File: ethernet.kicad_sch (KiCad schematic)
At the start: 37 parts, among them J801 SI-60062-F, U801 USBLC6-4SC6, U802 LAN8742A-CZ-TR, Y801 Crystal_GND24

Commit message: minor formatting updates
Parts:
- renumbered C811 to C801, C812 to C802, C801 to C803, C802 to C804, C803 to C805, C808 to C806, C809 to C807, C810 to C808, C806 to C809, C807 to C810, C804 to C811, C805 to C812, R810 to R801, R815 to R802, R816 to R803, R818 to R804, R819 to R805, R805 to R806, R806 to R807, R807 to R808, R820 to R809, R808 to R810, R809 to R811, R801 to R812, R802 to R813, R803 to R814, R817 to R815, R804 to R816, R811 to R817, R812 to R818, R813 to R819, R814 to R820, U802 to U801, U801 to U802

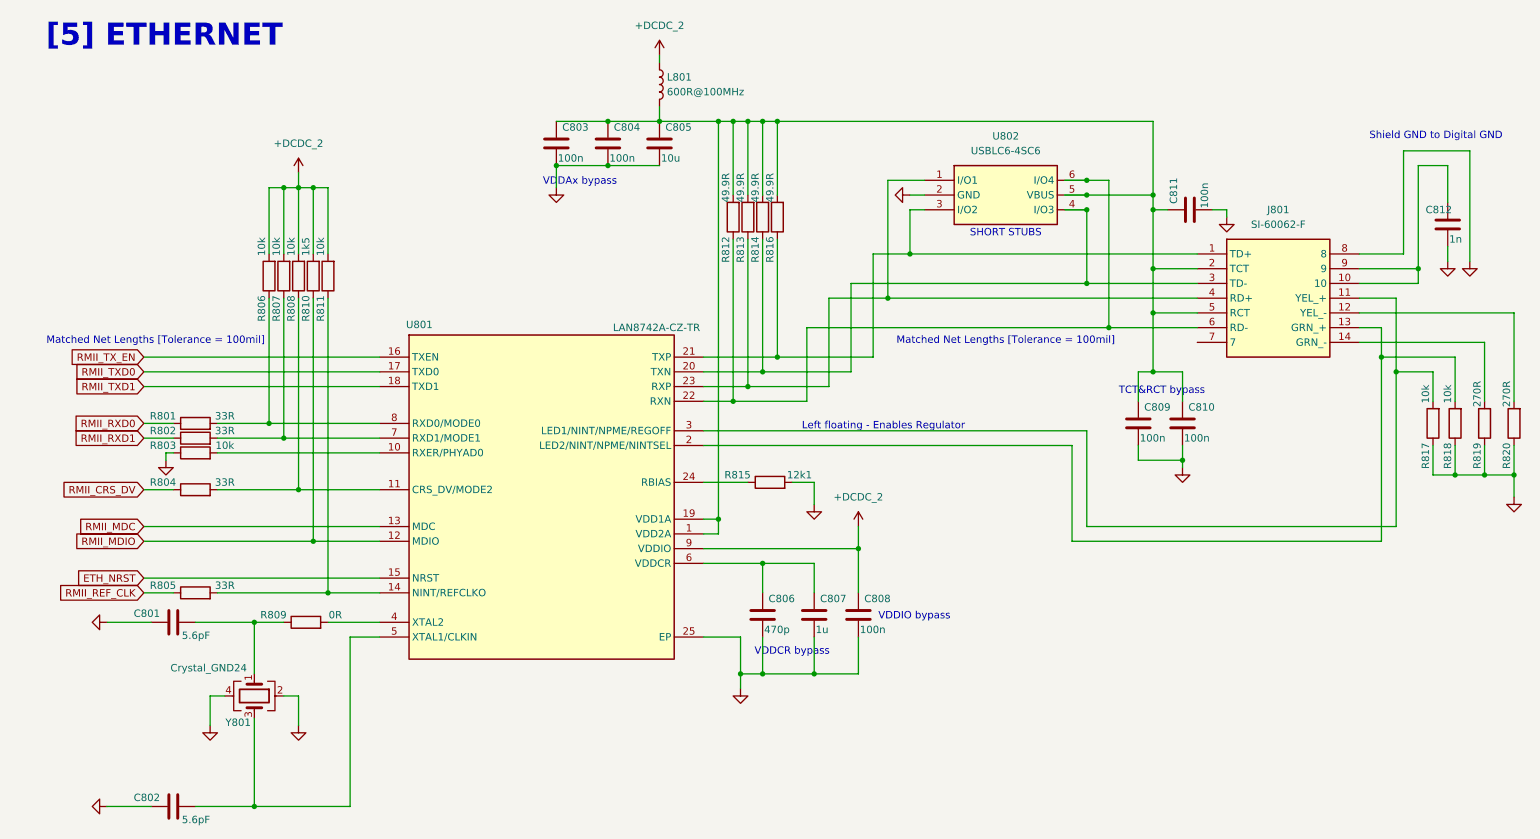
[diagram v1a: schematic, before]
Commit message: schematics errors fixed and ready for PCB
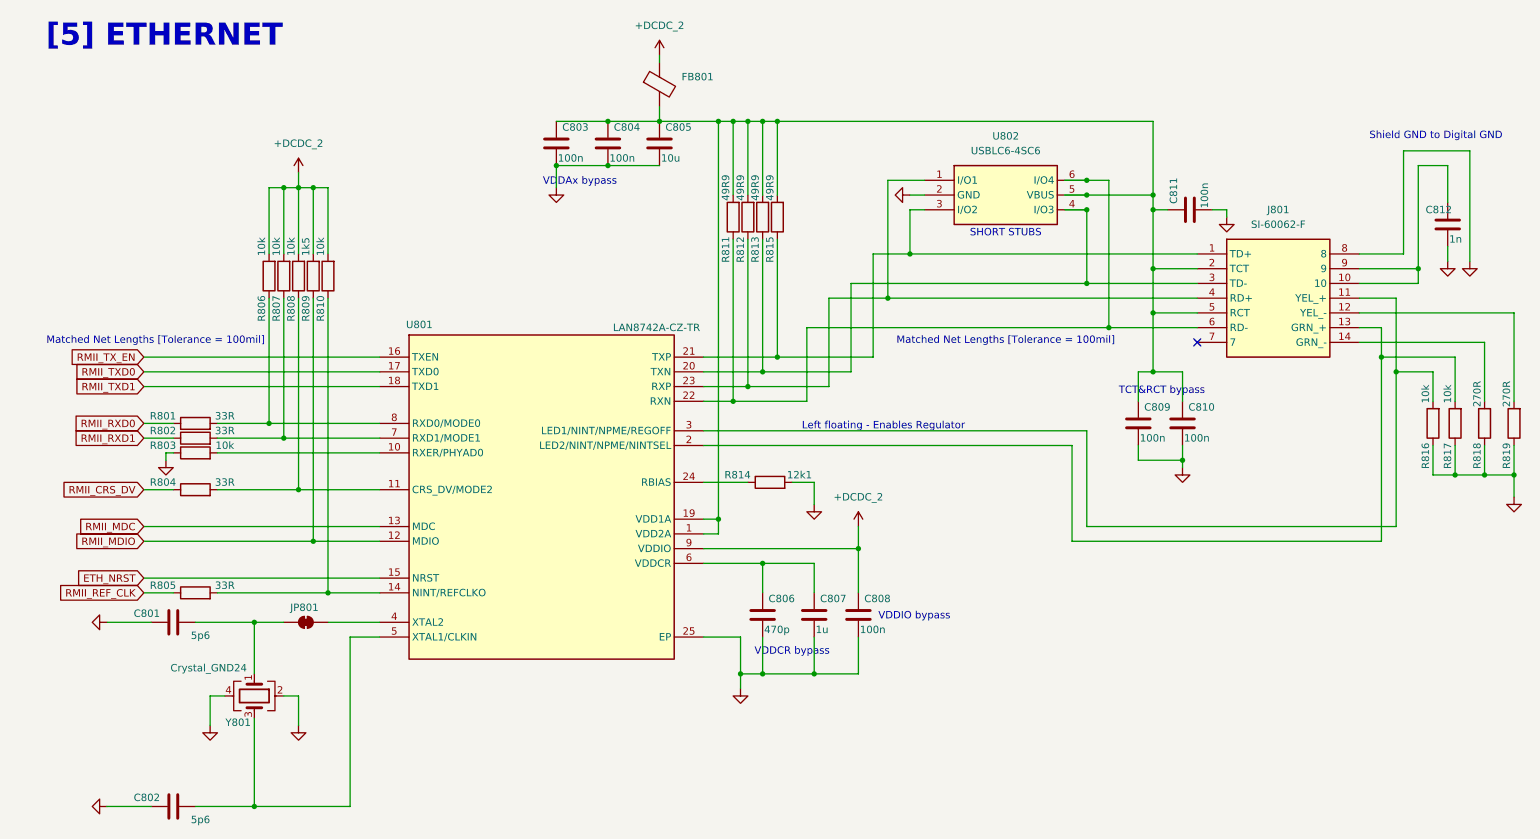
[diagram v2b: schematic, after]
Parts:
- removed L801: 600R@100MHz, symbol Device:L
- removed R809: 0R, symbol Device:R
- added FB801: FerriteBead, Inductor_SMD:L_0603_1608Metric, symbol Device:FerriteBead
- added JP801: SolderJumper_2_Bridged, Jumper:SolderJumper-2_P1.3mm_Bridged_RoundedPad1.0x1.5mm, symbol Jumper:SolderJumper_2_Bridged
- C801, C802: value 5.6pF -> 5p6; footprint (none) -> Capacitor_SMD:C_0402_1005Metric; Distributor_Link (none) -> https://www.mouser.com/ProductDetail/Murata-Electronics/GJM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; Manufacturer_Name (none) -> Murata Electronics; Manufacturer_Part_Number (none) -> GJM1555C1H5R6FB01D
- C803, C804, C808, C809, C810, C811: footprint (none) -> Capacitor_SMD:C_0402_1005Metric; Distributor_Link (none) -> https://www.mouser.com/ProductDetail/KYOCERA-AVX/04023C104K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; Manufacturer_Name (none) -> KYOCERA AVX; Manufacturer_Part_Number (none) -> 04023C104KAT2A
- C805: footprint (none) -> Capacitor_SMD:C_0603_1608Metric; Distributor_Link (none) -> https://www.mouser.com/ProductDetail/KYOCERA-AVX/KGM15CR51A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; Manufacturer_Name (none) -> KYOCERA AVX; Manufacturer_Part_Number (none) -> KGM15CR51A106KT
- C806: footprint (none) -> Capacitor_SMD:C_0402_1005Metric; Distributor_Link (none) -> https://www.mouser.com/ProductDetail/Murata-Electronics/GCM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; Manufacturer_Name (none) -> Murata Electronics; Manufacturer_Part_Number (none) -> GCM1555C2A471JE02D
- C807: footprint (none) -> Capacitor_SMD:C_0402_1005Metric; Distributor_Link (none) -> https://www.mouser.com/ProductDetail/KYOCERA-AVX/KGM05AR70J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; Manufacturer_Name (none) -> KYOCERA AVX; Manufacturer_Part_Number (none) -> KGM05AR70J105KH
- C812: footprint (none) -> Capacitor_SMD:C_0402_1005Metric; Distributor_Link (none) -> https://www.mouser.com/ProductDetail/Murata-Electronics/GCM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; Manufacturer_Name (none) -> Murata Electronics; Manufacturer_Part_Number (none) -> GCM1555C2A102JE02D
- R801, R802, R804, R805: footprint (none) -> Resistor_SMD:R_0603_1608Metric; Distributor_Link (none) -> https://www.mouser.com/ProductDetail/ROHM-Semiconductor/ESR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; Manufacturer_Name (none) -> ROHM Semiconductor; Manufacturer_Part_Number (none) -> ESR03EZPF33R0
- R803, R806, R807, R808: footprint (none) -> Resistor_SMD:R_0603_1608Metric; Distributor_Link (none) -> https://www.mouser.com/ProductDetail/Vishay-Dale/CRCW060310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; Manufacturer_Name (none) -> Vishay/Dale; Manufacturer_Part_Number (none) -> CRCW060310K0FKEI
- R809: renamed from R810; footprint (none) -> Resistor_SMD:R_0603_1608Metric; Distributor_Link (none) -> https://www.mouser.com/ProductDetail/TE-Connectivity-Holswo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; Manufacturer_Name (none) -> TE Connectivity; Manufacturer_Part_Number (none) -> RT73F1J1K5BTD
- R810: renamed from R811; footprint (none) -> Resistor_SMD:R_0603_1608Metric; Distributor_Link (none) -> https://www.mouser.com/ProductDetail/Vishay-Dale/CRCW060310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; Manufacturer_Name (none) -> Vishay/Dale; Manufacturer_Part_Number (none) -> CRCW060310K0FKEI
- R811: renamed from R812; value 49.9R -> 49R9; footprint (none) -> Resistor_SMD:R_0402_1005Metric; Distributor_Link (none) -> https://www.mouser.com/ProductDetail/Vishay/M55342K11B49D9R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; Manufacturer_Name (none) -> Vishay; Manufacturer_Part_Number (none) -> M55342K11B49D9RS2
- R812: renamed from R813; value 49.9R -> 49R9; footprint (none) -> Resistor_SMD:R_0402_1005Metric; Distributor_Link (none) -> https://www.mouser.com/ProductDetail/Vishay/M55342K11B49D9R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; Manufacturer_Name (none) -> Vishay; Manufacturer_Part_Number (none) -> M55342K11B49D9RS2
- R813: renamed from R814; value 49.9R -> 49R9; footprint (none) -> Resistor_SMD:R_0402_1005Metric; Distributor_Link (none) -> https://www.mouser.com/ProductDetail/Vishay/M55342K11B49D9R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; Manufacturer_Name (none) -> Vishay; Manufacturer_Part_Number (none) -> M55342K11B49D9RS2
- R814: renamed from R815; footprint (none) -> Resistor_SMD:R_0603_1608Metric; Distributor_Link (none) -> https://www.mouser.com/ProductDetail/Panasonic/ERJ-P03F1212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; Manufacturer_Name (none) -> Panasonic; Manufacturer_Part_Number (none) -> ERJ-P03F1212V
- R815: renamed from R816; value 49.9R -> 49R9; footprint (none) -> Resistor_SMD:R_0402_1005Metric; Distributor_Link (none) -> https://www.mouser.com/ProductDetail/Vishay/M55342K11B49D9R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; Manufacturer_Name (none) -> Vishay; Manufacturer_Part_Number (none) -> M55342K11B49D9RS2
- R816: renamed from R817; footprint (none) -> Resistor_SMD:R_0603_1608Metric; Distributor_Link (none) -> https://www.mouser.com/ProductDetail/Vishay-Dale/CRCW060310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; Manufacturer_Name (none) -> Vishay/Dale; Manufacturer_Part_Number (none) -> CRCW060310K0FKEI
- R817: renamed from R818; footprint (none) -> Resistor_SMD:R_0603_1608Metric; Distributor_Link (none) -> https://www.mouser.com/ProductDetail/Vishay-Dale/CRCW060310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; Manufacturer_Name (none) -> Vishay/Dale; Manufacturer_Part_Number (none) -> CRCW060310K0FKEI
- R818: renamed from R819; footprint (none) -> Resistor_SMD:R_0603_1608Metric; Distributor_Link (none) -> https://www.mouser.com/ProductDetail/YAGEO/TR0603NR-07270RL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; Manufacturer_Name (none) -> YAGEO; Manufacturer_Part_Number (none) -> TR0603NR-07270RL
- R819: renamed from R820; footprint (none) -> Resistor_SMD:R_0603_1608Metric; Distributor_Link (none) -> https://www.mouser.com/ProductDetail/YAGEO/TR0603NR-07270RL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; Manufacturer_Name (none) -> YAGEO; Manufacturer_Part_Number (none) -> TR0603NR-07270RL
- U801: Distributor_Link (none) -> https://www.mouser.com/ProductDetail/Microchip-Technology/L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
- U802: Distributor_Link (none) -> https://www.mouser.com/ProductDetail/STMicroelectronics/USB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
- Y801: Distributor_Link (none) -> https://www.mouser.com/ProductDetail/NDK/NX3225SA-25.000M-S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; Manufacturer_Name (none) -> NDK; Manufacturer_Part_Number (none) -> NX3225SA-25.000M-STD-CSR-6
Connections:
- net +DCDC_2: now also FB801.1
- net at C803.1, C804.1, C805.1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: now also FB801.2
- net at C801.2, Y801.1: now also JP801.1 (A)
- net at U801.4 (XTAL2): now also JP801.2 (B)
- no-connect marks 0 -> 1

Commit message: new version created. Now at v2.0.0
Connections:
- net RMII_TXP: now reaches J801.1 (TD+), R815.1, U801.21 (TXP), U802.3 (I/O2)
- net ETH_DCDC2_FR: now reaches C803.1, C804.1, C805.1, C809.1, C810.1, C811.1, FB801.2, J801.2 (TCT), J801.5 (RCT), R811.2, R812.2, R813.2, R815.2, U801.1 (VDD2A), U801.19 (VDD1A), U802.5 (VBUS)
- net RMII_TXN: now reaches J801.3 (TD-), R813.1, U801.20 (TXN), U802.4 (I/O3)
- net RMII_RXD1_R: now reaches R802.2, R807.1, U801.7 (RXD1/MODE1)
- net RMII_REF_CLK_R: now reaches R805.2, R810.1, U801.14 (NINT/REFCLKO)
- net RMII_CRS_DV_R: now reaches R804.2, R808.1, U801.11 (CRS_DV/MODE2)
- net RMII_XTAL2: now reaches JP801.2 (B), U801.4 (XTAL2)
- net RMII_PHYAD0: now reaches R803.2, U801.10 (RXER/PHYAD0)
- net RMII_XTAL1: now reaches C802.2, U801.5 (XTAL1/CLKIN), Y801.3
- net RMII_RXP: now reaches J801.4 (RD+), R812.1, U801.23 (RXP), U802.1 (I/O1)
- net RMII_RXN: now reaches J801.6 (RD-), R811.1, U801.22 (RXN), U802.6 (I/O4)
- net RMII_RXD0_R: now reaches R801.2, R806.1, U801.8 (RXD0/MODE0)
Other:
- moved on the sheet: JP801
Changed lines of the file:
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@@
+	(wire
+		(pts
+			(xy 53.34 86.36) (xy 72.39 86.36)
+		)
+		(stroke
+			(width 0)
+			(type default)
+		)
+	)
 	(wire
 		(pts
@@
 	(wire
 		(pts
-			(xy 63.5 120.65) (xy 72.39 120.65)
-		)
-		(stroke
-			(width 0)
-			(type default)
-		)
-	)
-	(wire
-		(pts
 			(xy 60.96 106.68) (xy 72.39 106.68)
 		)
@@
 	(wire
 		(pts
+			(xy 60.96 120.65) (xy 72.39 120.65)
+		)
+		(stroke
+			(width 0)
+			(type default)
+		)
+	)
+	(wire
+		(pts
 			(xy 140.97 34.29) (xy 140.97 46.99)
 		)
@@
 	(wire
 		(pts
-			(xy 50.8 120.65) (xy 55.88 120.65)
+			(xy 50.8 120.65) (xy 53.34 120.65)
 		)
 		(stroke
@@
 		(pts
 			(xy 241.3 57.15) (xy 248.92 57.15)
-		)
-		(stroke
-			(width 0)
-			(type default)
-		)
-	)
-	(wire
-		(pts
-			(xy 53.34 86.36) (xy 72.39 86.36)
 		)
 		(stroke
@@
 				(size 1.27 1.27)
 			)
+		)
+	)
+	(label "RMII_RXP"
+		(at 149.86 80.01 0)
+		(fields_autoplaced yes)
+		(effects
+			(font
+				(size 1.27 1.27)
+			)
+			(justify left bottom)
+		)
+	)
+	(label "RMII_RXD1_R"
+		(at 49.53 88.9 0)
+		(fields_autoplaced yes)
+		(effects
+			(font
+				(size 1.27 1.27)
+			)
+			(justify left bottom)
+		)
+	)
+	(label "RMII_RXD0_R"
+		(at 49.53 86.36 0)
+		(fields_autoplaced yes)
+		(effects
+			(font
+				(size 1.27 1.27)
+			)
+			(justify left bottom)
+		)
+	)
+	(label "RMII_TXP"
+		(at 157.48 74.93 0)
+		(fields_autoplaced yes)
+		(effects
+			(font
+				(size 1.27 1.27)
+			)
+			(justify left bottom)
+		)
+	)
+	(label "RMII_REF_CLK_R"
+		(at 53.34 115.57 0)
+		(fields_autoplaced yes)
+		(effects
+			(font
+				(size 1.27 1.27)
+			)
+			(justify left bottom)
+		)
+	)
+	(label "RMII_CRS_DV_R"
+		(at 49.53 97.79 0)
+		(fields_autoplaced yes)
+		(effects
+			(font
+				(size 1.27 1.27)
+			)
+			(justify left bottom)
+		)
+	)
+	(label "RMII_XTAL1"
+		(at 69.85 123.19 180)
+		(fields_autoplaced yes)
+		(effects
+			(font
+				(size 1.27 1.27)
+			)
+			(justify right bottom)
+		)
+	)
+	(label "RMII_RXN"
+		(at 146.05 82.55 0)
+		(fields_autoplaced yes)
+		(effects
+			(font
+				(size 1.27 1.27)
+			)
+			(justify left bottom)
+		)
+	)
+	(label "RMII_XTAL2"
+		(at 60.96 120.65 0)
+		(fields_autoplaced yes)
+		(effects
+			(font
+				(size 1.27 1.27)
+			)
+			(justify left bottom)
+		)
+	)
+	(label "RMII_TXN"
+		(at 153.67 77.47 0)
+		(fields_autoplaced yes)
+		(effects
+			(font
+				(size 1.27 1.27)
+			)
+			(justify left bottom)
+		)
+	)
+	(label "RMII_PHYAD0"
+		(at 49.53 91.44 0)
+		(fields_autoplaced yes)
+		(effects
+			(font
+				(size 1.27 1.27)
+			)
+			(justify left bottom)
+		)
+	)
+	(label "ETH_DCDC2_FR"
+		(at 148.59 34.29 0)
+		(fields_autoplaced yes)
+		(effects
+			(font
+				(size 1.27 1.27)
+			)
+			(justify left bottom)
 		)
 	)
@@
 	(symbol
 		(lib_id "Jumper:SolderJumper_2_Bridged")
-		(at 59.69 120.65 0)
+		(at 57.15 120.65 0)
 		(unit 1)
 		(exclude_from_sim yes)
@@
 		(dnp no)
 		(property "Reference" "JP801"
-			(at 59.436 118.11 0)
+			(at 56.896 118.11 0)
 			(effects
 				(font
@@
 		)
 		(property "Value" "SolderJumper_2_Bridged"
-			(at 59.69 116.84 0)
+			(at 57.15 116.84 0)
 			(effects
 				(font
@@
 		)
 		(property "Footprint" "Jumper:SolderJumper-2_P1.3mm_Bridged_RoundedPad1.0x1.5mm"
-			(at 59.69 120.65 0)
+			(at 57.15 120.65 0)
 			(effects
 				(font
@@
 		)
 		(property "Datasheet" "~"
-			(at 59.69 120.65 0)
+			(at 57.15 120.65 0)
 			(effects
 				(font
@@
 		)
 		(property "Description" "Solder Jumper, 2-pole, closed/bridged"
-			(at 59.69 120.65 0)
-			(effects
-				(font
+			(at 57.15 120.65 0)
+			(effects
+				(font
